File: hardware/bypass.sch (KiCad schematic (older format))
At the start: 12 parts

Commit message: Assign project specific footprints
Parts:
- REL? (x3): footprint (none) -> uMIDI-FX:Omron_G6K-2G
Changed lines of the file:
@@
 $Descr A4 11693 8268
 encoding utf-8
-Sheet 14 21
+Sheet 5 21
 Title ""
 Date ""
@@
 F 0 "REL?" H 8050 3500 60  0000 C CNN
 F 1 "Omron G6K-2G-5VCD" H 8050 3600 60  0000 C CNN
-F 2 "" H 8050 3300 60  0000 C CNN
+F 2 "uMIDI-FX:Omron_G6K-2G" H 8050 3300 60  0001 C CNN
 F 3 "" H 8050 3300 60  0000 C CNN
 	1    8050 3300
@@
 F 0 "REL?" H 3700 4000 60  0000 C CNN
 F 1 "Omron G6K-2G-5VCD" H 3700 3500 60  0001 C CNN
-F 2 "" H 3700 3800 60  0000 C CNN
+F 2 "uMIDI-FX:Omron_G6K-2G" H 3700 3800 60  0001 C CNN
 F 3 "" H 3700 3800 60  0000 C CNN
 	2    3700 3800
@@
 F 0 "REL?" H 5200 4000 60  0000 C CNN
 F 1 "Omron G6K-2G-5VCD" H 4850 4150 60  0001 C CNN
-F 2 "" H 5200 3800 60  0000 C CNN
+F 2 "uMIDI-FX:Omron_G6K-2G" H 5200 3800 60  0001 C CNN
 F 3 "" H 5200 3800 60  0000 C CNN
 	3    5200 3800

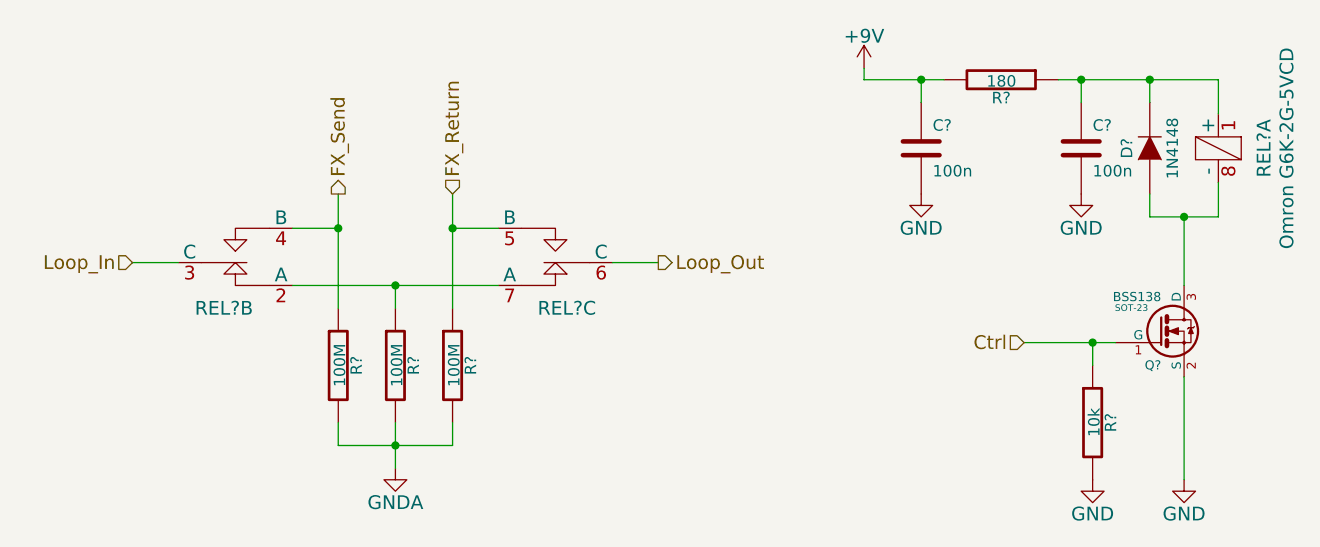
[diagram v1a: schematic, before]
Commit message: Annotate schematic components
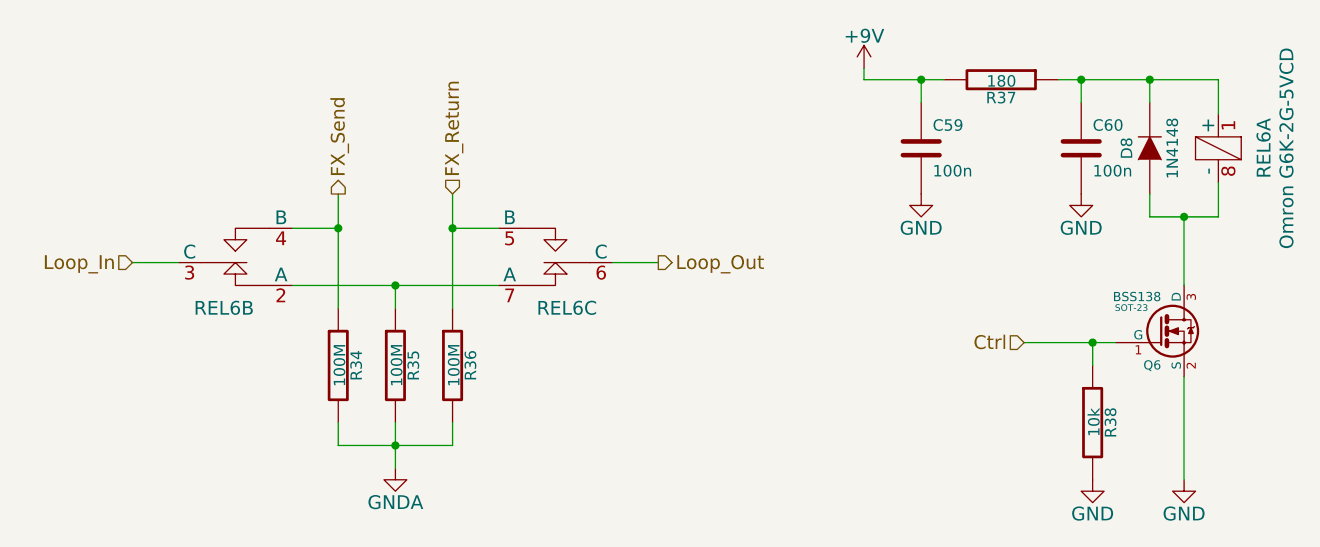
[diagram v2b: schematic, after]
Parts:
- gave numbers to parts that had none: 10

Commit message: Replace barrel jack symbols
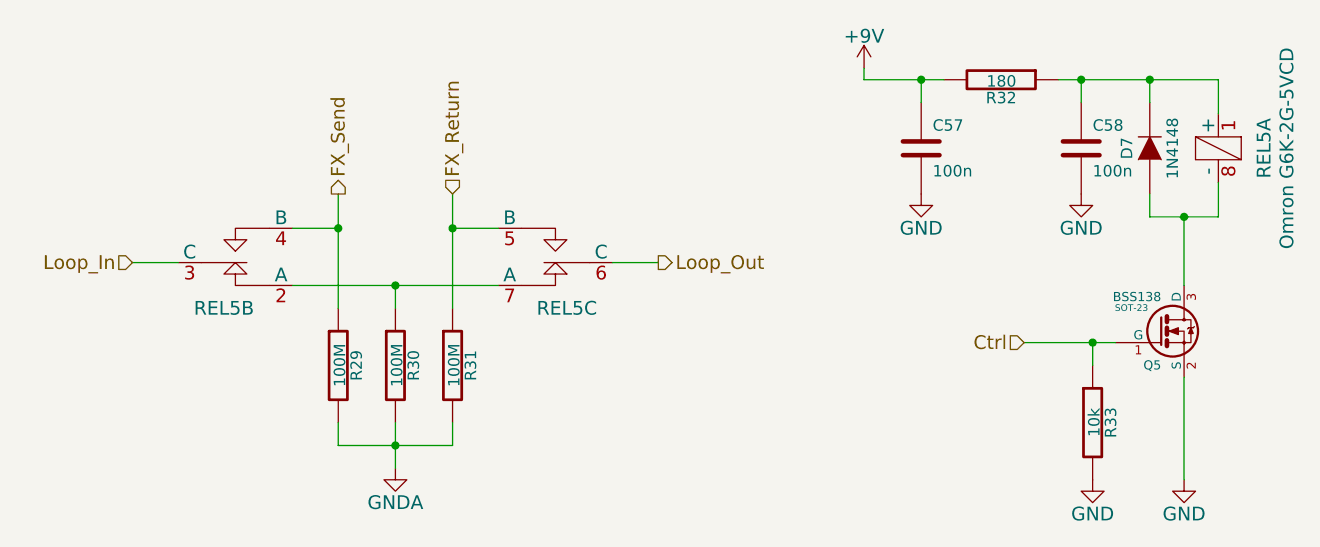
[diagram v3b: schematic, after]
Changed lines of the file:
@@
 $Descr A4 11693 8268
 encoding utf-8
-Sheet 15 21
+Sheet 13 21
 Title ""
 Date ""
@@
 AR Path="/54D120FF/54EA08CB/54E9BE9F/54D79A29" Ref="REL7"  Part="1"
 AR Path="/54D120FF/54E9FD8E/54E9BE9F/54D79A29" Ref="REL4"  Part="1"
-F 0 "REL6" H 8050 3500 60  0000 C CNN
+F 0 "REL5" H 8050 3500 60  0000 C CNN
 F 1 "Omron G6K-2G-5VCD" H 8050 3600 60  0000 C CNN
 F 2 "uMIDI-FX:Omron_G6K-2G" H 8050 3300 60  0001 C CNN
@@
 AR Path="/54D120FF/54EA08CB/54E9BE9F/54D79A79" Ref="REL7"  Part="2"
 AR Path="/54D120FF/54E9FD8E/54E9BE9F/54D79A79" Ref="REL4"  Part="2"
-F 0 "REL6" H 3700 4000 60  0000 C CNN
+F 0 "REL5" H 3700 4000 60  0000 C CNN
 F 1 "Omron G6K-2G-5VCD" H 3700 3500 60  0001 C CNN
 F 2 "uMIDI-FX:Omron_G6K-2G" H 3700 3800 60  0001 C CNN
@@
 AR Path="/54D120FF/54EA08CB/54E9BE9F/54D79AAA" Ref="REL7"  Part="3"
 AR Path="/54D120FF/54E9FD8E/54E9BE9F/54D79AAA" Ref="REL4"  Part="3"
-F 0 "REL6" H 5200 4000 60  0000 C CNN
+F 0 "REL5" H 5200 4000 60  0000 C CNN
 F 1 "Omron G6K-2G-5VCD" H 4850 4150 60  0001 C CNN
 F 2 "uMIDI-FX:Omron_G6K-2G" H 5200 3800 60  0001 C CNN
@@
 AR Path="/54D120FF/54EA08CB/54E9BE9F/54D79DA0" Ref="R39"  Part="1"
 AR Path="/54D120FF/54E9FD8E/54E9BE9F/54D79DA0" Ref="R24"  Part="1"
-F 0 "R34" V 4280 4250 50  0000 C CNN
+F 0 "R29" V 4280 4250 50  0000 C CNN
 F 1 "100M" V 4207 4251 50  0000 C CNN
 F 2 "" V 4130 4250 30  0000 C CNN
@@
 AR Path="/54D120FF/54EA08CB/54E9BE9F/54D79EDE" Ref="R41"  Part="1"
 AR Path="/54D120FF/54E9FD8E/54E9BE9F/54D79EDE" Ref="R26"  Part="1"
-F 0 "R36" V 4780 4250 50  0000 C CNN
+F 0 "R31" V 4780 4250 50  0000 C CNN
 F 1 "100M" V 4707 4251 50  0000 C CNN
 F 2 "" V 4630 4250 30  0000 C CNN
@@
 AR Path="/54D120FF/54EA08CB/54E9BE9F/54D79F11" Ref="R40"  Part="1"
 AR Path="/54D120FF/54E9FD8E/54E9BE9F/54D79F11" Ref="R25"  Part="1"
-F 0 "R35" V 4530 4250 50  0000 C CNN
+F 0 "R30" V 4530 4250 50  0000 C CNN
 F 1 "100M" V 4457 4251 50  0000 C CNN
 F 2 "" V 4380 4250 30  0000 C CNN
@@
 AR Path="/54D120FF/54EA08CB/54E9BE9F/54D7A6A7" Ref="D9"  Part="1"
 AR Path="/54D120FF/54E9FD8E/54E9BE9F/54D7A6A7" Ref="D6"  Part="1"
-F 0 "D8" H 7750 3400 50  0000 C CNN
+F 0 "D7" H 7750 3400 50  0000 C CNN
 F 1 "1N4148" H 7750 3200 50  0000 C CNN
 F 2 "" H 7750 3300 60  0000 C CNN
@@
 AR Path="/54D120FF/54EA08CB/54E9BE9F/54D7A960" Ref="#PWR122"  Part="1"
 AR Path="/54D120FF/54E9FD8E/54E9BE9F/54D7A960" Ref="#PWR101"  Part="1"
-F 0 "#PWR115" H 7900 4500 60  0001 C CNN
+F 0 "#PWR108" H 7900 4500 60  0001 C CNN
 F 1 "GND" H 7900 4600 60  0000 C CNN
 F 2 "" H 7900 4750 60  0000 C CNN
@@
 AR Path="/54D120FF/54EA08CB/54E9BE9F/54D7AAB4" Ref="C61"  Part="1"
 AR Path="/54D120FF/54E9FD8E/54E9BE9F/54D7AAB4" Ref="C55"  Part="1"
-F 0 "C59" H 6800 3400 50  0000 L CNN
+F 0 "C57" H 6800 3400 50  0000 L CNN
 F 1 "100n" H 6800 3200 50  0000 L CNN
 F 2 "" H 6788 3150 30  0000 C CNN
@@
 AR Path="/54D120FF/54EA08CB/54E9BE9F/54D7AB88" Ref="#PWR119"  Part="1"
 AR Path="/54D120FF/54E9FD8E/54E9BE9F/54D7AB88" Ref="#PWR98"  Part="1"
-F 0 "#PWR112" H 6750 3250 60  0001 C CNN
+F 0 "#PWR105" H 6750 3250 60  0001 C CNN
 F 1 "GND" H 6750 3350 60  0000 C CNN
 F 2 "" H 6750 3500 60  0000 C CNN
@@
 AR Path="/54D120FF/54EA08CB/54E9BE9F/54D7ADF3" Ref="R43"  Part="1"
 AR Path="/54D120FF/54E9FD8E/54E9BE9F/54D7ADF3" Ref="R28"  Part="1"
-F 0 "R38" V 7580 4500 50  0000 C CNN
+F 0 "R33" V 7580 4500 50  0000 C CNN
 F 1 "10k" V 7507 4501 50  0000 C CNN
 F 2 "" V 7430 4500 30  0000 C CNN
@@
 AR Path="/54D120FF/54EA08CB/54E9BE9F/54D7AECB" Ref="Q7"  Part="1"
 AR Path="/54D120FF/54E9FD8E/54E9BE9F/54D7AECB" Ref="Q4"  Part="1"
-F 0 "Q6" H 7800 3951 40  0000 R CNN
+F 0 "Q5" H 7800 3951 40  0000 R CNN
 F 1 "BSS138" H 7800 4250 40  0000 R CNN
 F 2 "SOT-23" H 7670 4202 29  0000 C CNN
@@
 AR Path="/54D120FF/54EA08CB/54E9BE9F/54D7B0C5" Ref="#PWR121"  Part="1"
 AR Path="/54D120FF/54E9FD8E/54E9BE9F/54D7B0C5" Ref="#PWR100"  Part="1"
-F 0 "#PWR114" H 7500 4500 60  0001 C CNN
+F 0 "#PWR107" H 7500 4500 60  0001 C CNN
 F 1 "GND" H 7500 4600 60  0000 C CNN
 F 2 "" H 7500 4750 60  0000 C CNN
@@
 AR Path="/54D120FF/54EA08CB/54E9BE9F/54D7C711" Ref="R42"  Part="1"
 AR Path="/54D120FF/54E9FD8E/54E9BE9F/54D7C711" Ref="R27"  Part="1"
-F 0 "R37" V 7180 3000 50  0000 C CNN
+F 0 "R32" V 7180 3000 50  0000 C CNN
 F 1 "180" V 7107 3001 50  0000 C CNN
 F 2 "" V 7030 3000 30  0000 C CNN
@@
 AR Path="/54D120FF/54EA08CB/54E9BE9F/54D7C874" Ref="C62"  Part="1"
 AR Path="/54D120FF/54E9FD8E/54E9BE9F/54D7C874" Ref="C56"  Part="1"
-F 0 "C60" H 7500 3400 50  0000 L CNN
+F 0 "C58" H 7500 3400 50  0000 L CNN
 F 1 "100n" H 7500 3200 50  0000 L CNN
 F 2 "" H 7488 3150 30  0000 C CNN
@@
 AR Path="/54D120FF/54EA08CB/54E9BE9F/54D7C87A" Ref="#PWR120"  Part="1"
 AR Path="/54D120FF/54E9FD8E/54E9BE9F/54D7C87A" Ref="#PWR99"  Part="1"
-F 0 "#PWR113" H 7450 3250 60  0001 C CNN
+F 0 "#PWR106" H 7450 3250 60  0001 C CNN
 F 1 "GND" H 7450 3350 60  0000 C CNN
 F 2 "" H 7450 3500 60  0000 C CNN
@@
 AR Path="/54D120FF/54E9FD8E/54E9BE9F/54EA1C00" Ref="#PWR96"  Part="1"
 AR Path="/54D120FF/54E9BE87/54E9BE9F/54EA1C00" Ref="#PWR124"  Part="1"
-F 0 "#PWR110" H 4450 4450 60  0001 C CNN
+F 0 "#PWR103" H 4450 4450 60  0001 C CNN
 F 1 "GNDA" H 4450 4550 60  0000 C CNN
 F 2 "" H 4450 4700 60  0000 C CNN
@@
 AR Path="/54D120FF/54E9FD8E/54E9BE9F/54E940D4" Ref="#PWR97"  Part="1"
 AR Path="/54D120FF/54E9BE87/54E9BE9F/54E940D4" Ref="#PWR125"  Part="1"
-F 0 "#PWR111" H 6500 2800 60  0001 C CNN
+F 0 "#PWR104" H 6500 2800 60  0001 C CNN
 F 1 "+9V" H 6500 3090 60  0000 C CNN
 F 2 "" H 6500 2950 60  0000 C CNN

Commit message: Set footprint of catch diode; Add datasheet
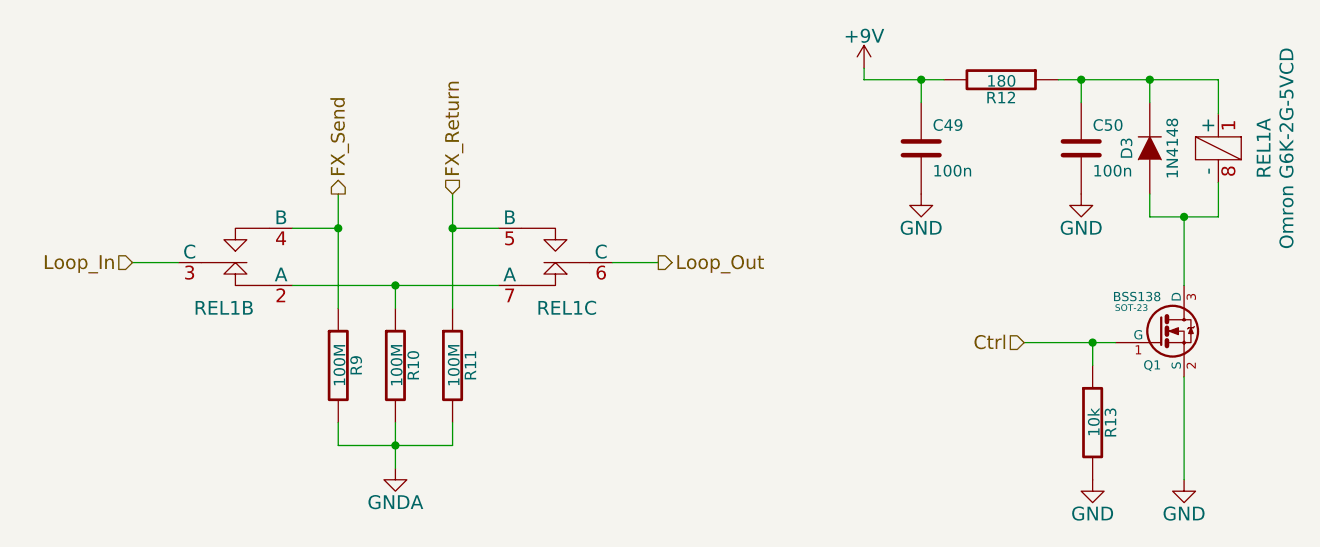
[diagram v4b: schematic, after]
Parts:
- D3: footprint (none) -> Diodes_SMD:SOD-323
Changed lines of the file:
@@
 $Descr A4 11693 8268
 encoding utf-8
-Sheet 13 21
+Sheet 5 21
 Title ""
 Date ""
@@
 AR Path="/54D120FF/54EA08CB/54E9BE9F/54D79A29" Ref="REL7"  Part="1"
 AR Path="/54D120FF/54E9FD8E/54E9BE9F/54D79A29" Ref="REL4"  Part="1"
-F 0 "REL5" H 8050 3500 60  0000 C CNN
+F 0 "REL1" H 8050 3500 60  0000 C CNN
 F 1 "Omron G6K-2G-5VCD" H 8050 3600 60  0000 C CNN
 F 2 "uMIDI-FX:Omron_G6K-2G" H 8050 3300 60  0001 C CNN
@@
 AR Path="/54D120FF/54EA08CB/54E9BE9F/54D79A79" Ref="REL7"  Part="2"
 AR Path="/54D120FF/54E9FD8E/54E9BE9F/54D79A79" Ref="REL4"  Part="2"
-F 0 "REL5" H 3700 4000 60  0000 C CNN
+F 0 "REL1" H 3700 4000 60  0000 C CNN
 F 1 "Omron G6K-2G-5VCD" H 3700 3500 60  0001 C CNN
 F 2 "uMIDI-FX:Omron_G6K-2G" H 3700 3800 60  0001 C CNN
@@
 AR Path="/54D120FF/54EA08CB/54E9BE9F/54D79AAA" Ref="REL7"  Part="3"
 AR Path="/54D120FF/54E9FD8E/54E9BE9F/54D79AAA" Ref="REL4"  Part="3"
-F 0 "REL5" H 5200 4000 60  0000 C CNN
+F 0 "REL1" H 5200 4000 60  0000 C CNN
 F 1 "Omron G6K-2G-5VCD" H 4850 4150 60  0001 C CNN
 F 2 "uMIDI-FX:Omron_G6K-2G" H 5200 3800 60  0001 C CNN
@@
 AR Path="/54D120FF/54EA08CB/54E9BE9F/54D79DA0" Ref="R39"  Part="1"
 AR Path="/54D120FF/54E9FD8E/54E9BE9F/54D79DA0" Ref="R24"  Part="1"
-F 0 "R29" V 4280 4250 50  0000 C CNN
+F 0 "R9" V 4280 4250 50  0000 C CNN
 F 1 "100M" V 4207 4251 50  0000 C CNN
 F 2 "" V 4130 4250 30  0000 C CNN
@@
 AR Path="/54D120FF/54EA08CB/54E9BE9F/54D79EDE" Ref="R41"  Part="1"
 AR Path="/54D120FF/54E9FD8E/54E9BE9F/54D79EDE" Ref="R26"  Part="1"
-F 0 "R31" V 4780 4250 50  0000 C CNN
+F 0 "R11" V 4780 4250 50  0000 C CNN
 F 1 "100M" V 4707 4251 50  0000 C CNN
 F 2 "" V 4630 4250 30  0000 C CNN
@@
 AR Path="/54D120FF/54EA08CB/54E9BE9F/54D79F11" Ref="R40"  Part="1"
 AR Path="/54D120FF/54E9FD8E/54E9BE9F/54D79F11" Ref="R25"  Part="1"
-F 0 "R30" V 4530 4250 50  0000 C CNN
+F 0 "R10" V 4530 4250 50  0000 C CNN
 F 1 "100M" V 4457 4251 50  0000 C CNN
 F 2 "" V 4380 4250 30  0000 C CNN
@@
 AR Path="/54D120FF/54EA08CB/54E9BE9F/54D7A6A7" Ref="D9"  Part="1"
 AR Path="/54D120FF/54E9FD8E/54E9BE9F/54D7A6A7" Ref="D6"  Part="1"
-F 0 "D7" H 7750 3400 50  0000 C CNN
+F 0 "D3" H 7750 3400 50  0000 C CNN
 F 1 "1N4148" H 7750 3200 50  0000 C CNN
-F 2 "" H 7750 3300 60  0000 C CNN
+F 2 "Diodes_SMD:SOD-323" H 7750 3300 60  0001 C CNN
 F 3 "" H 7750 3300 60  0000 C CNN
 	1    7750 3300
@@
 AR Path="/54D120FF/54EA08CB/54E9BE9F/54D7A960" Ref="#PWR122"  Part="1"
 AR Path="/54D120FF/54E9FD8E/54E9BE9F/54D7A960" Ref="#PWR101"  Part="1"
-F 0 "#PWR108" H 7900 4500 60  0001 C CNN
+F 0 "#PWR77" H 7900 4500 60  0001 C CNN
 F 1 "GND" H 7900 4600 60  0000 C CNN
 F 2 "" H 7900 4750 60  0000 C CNN
@@
 AR Path="/54D120FF/54EA08CB/54E9BE9F/54D7AAB4" Ref="C61"  Part="1"
 AR Path="/54D120FF/54E9FD8E/54E9BE9F/54D7AAB4" Ref="C55"  Part="1"
-F 0 "C57" H 6800 3400 50  0000 L CNN
+F 0 "C49" H 6800 3400 50  0000 L CNN
 F 1 "100n" H 6800 3200 50  0000 L CNN
 F 2 "" H 6788 3150 30  0000 C CNN
@@
 AR Path="/54D120FF/54EA08CB/54E9BE9F/54D7AB88" Ref="#PWR119"  Part="1"
 AR Path="/54D120FF/54E9FD8E/54E9BE9F/54D7AB88" Ref="#PWR98"  Part="1"
-F 0 "#PWR105" H 6750 3250 60  0001 C CNN
+F 0 "#PWR74" H 6750 3250 60  0001 C CNN
 F 1 "GND" H 6750 3350 60  0000 C CNN
 F 2 "" H 6750 3500 60  0000 C CNN
@@
 AR Path="/54D120FF/54EA08CB/54E9BE9F/54D7ADF3" Ref="R43"  Part="1"
 AR Path="/54D120FF/54E9FD8E/54E9BE9F/54D7ADF3" Ref="R28"  Part="1"
-F 0 "R33" V 7580 4500 50  0000 C CNN
+F 0 "R13" V 7580 4500 50  0000 C CNN
 F 1 "10k" V 7507 4501 50  0000 C CNN
 F 2 "" V 7430 4500 30  0000 C CNN
@@
 AR Path="/54D120FF/54EA08CB/54E9BE9F/54D7AECB" Ref="Q7"  Part="1"
 AR Path="/54D120FF/54E9FD8E/54E9BE9F/54D7AECB" Ref="Q4"  Part="1"
-F 0 "Q5" H 7800 3951 40  0000 R CNN
+F 0 "Q1" H 7800 3951 40  0000 R CNN
 F 1 "BSS138" H 7800 4250 40  0000 R CNN
 F 2 "SOT-23" H 7670 4202 29  0000 C CNN
@@
 AR Path="/54D120FF/54EA08CB/54E9BE9F/54D7B0C5" Ref="#PWR121"  Part="1"
 AR Path="/54D120FF/54E9FD8E/54E9BE9F/54D7B0C5" Ref="#PWR100"  Part="1"
-F 0 "#PWR107" H 7500 4500 60  0001 C CNN
+F 0 "#PWR76" H 7500 4500 60  0001 C CNN
 F 1 "GND" H 7500 4600 60  0000 C CNN
 F 2 "" H 7500 4750 60  0000 C CNN
@@
 AR Path="/54D120FF/54EA08CB/54E9BE9F/54D7C711" Ref="R42"  Part="1"
 AR Path="/54D120FF/54E9FD8E/54E9BE9F/54D7C711" Ref="R27"  Part="1"
-F 0 "R32" V 7180 3000 50  0000 C CNN
+F 0 "R12" V 7180 3000 50  0000 C CNN
 F 1 "180" V 7107 3001 50  0000 C CNN
 F 2 "" V 7030 3000 30  0000 C CNN
@@
 AR Path="/54D120FF/54EA08CB/54E9BE9F/54D7C874" Ref="C62"  Part="1"
 AR Path="/54D120FF/54E9FD8E/54E9BE9F/54D7C874" Ref="C56"  Part="1"
-F 0 "C58" H 7500 3400 50  0000 L CNN
+F 0 "C50" H 7500 3400 50  0000 L CNN
 F 1 "100n" H 7500 3200 50  0000 L CNN
 F 2 "" H 7488 3150 30  0000 C CNN
@@
 AR Path="/54D120FF/54EA08CB/54E9BE9F/54D7C87A" Ref="#PWR120"  Part="1"
 AR Path="/54D120FF/54E9FD8E/54E9BE9F/54D7C87A" Ref="#PWR99"  Part="1"
-F 0 "#PWR106" H 7450 3250 60  0001 C CNN
+F 0 "#PWR75" H 7450 3250 60  0001 C CNN
 F 1 "GND" H 7450 3350 60  0000 C CNN
 F 2 "" H 7450 3500 60  0000 C CNN
@@
 AR Path="/54D120FF/54E9FD8E/54E9BE9F/54EA1C00" Ref="#PWR96"  Part="1"
 AR Path="/54D120FF/54E9BE87/54E9BE9F/54EA1C00" Ref="#PWR124"  Part="1"
-F 0 "#PWR103" H 4450 4450 60  0001 C CNN
+F 0 "#PWR72" H 4450 4450 60  0001 C CNN
 F 1 "GNDA" H 4450 4550 60  0000 C CNN
 F 2 "" H 4450 4700 60  0000 C CNN
@@
 AR Path="/54D120FF/54E9FD8E/54E9BE9F/54E940D4" Ref="#PWR97"  Part="1"
 AR Path="/54D120FF/54E9BE87/54E9BE9F/54E940D4" Ref="#PWR125"  Part="1"
-F 0 "#PWR104" H 6500 2800 60  0001 C CNN
+F 0 "#PWR73" H 6500 2800 60  0001 C CNN
 F 1 "+9V" H 6500 3090 60  0000 C CNN
 F 2 "" H 6500 2950 60  0000 C CNN
